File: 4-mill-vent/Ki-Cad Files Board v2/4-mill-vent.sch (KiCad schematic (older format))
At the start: 73 parts, among them J1 Fan, J2 Buzzer, J3 Power, J4 ICSP, J9 Mounting holes, Q3 PZT3904, Q4 PZT3904, Q5 TSM480P06CP, Q6 MMBT3904, SW1 Power_off, SW2 Power_On, SW3 Fan_Down, SW4 Fan_Up, U1 LM321, U2 ATmega328P-AU, U3 TPSM84212EAB, U4 LM1117-5.0, Y1 16.000MHZ

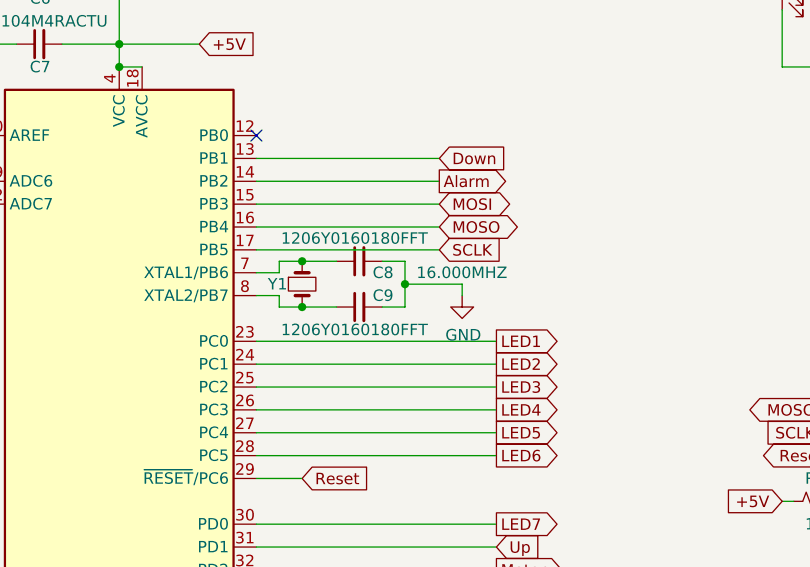
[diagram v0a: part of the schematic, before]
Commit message: Last Update USE V2
Board test complete, all slikscreen error are fixed in v2, Full use of opamp for battery monitoring.
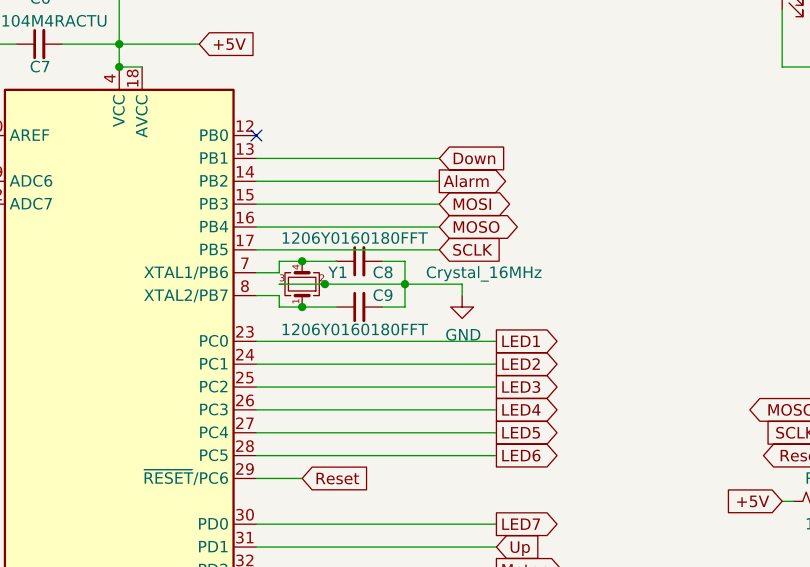
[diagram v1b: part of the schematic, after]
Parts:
- removed Y1: 16.000MHZ, Crystal:Crystal_SMD_0603-2Pin_6.0x3.5mm, symbol Device:Crystal_Small
- added Y1: Crystal_16MHz, Crystal:Crystal_SMD_0603-4Pin_6.0x3.5mm, symbol Device:Crystal_GND23_Small
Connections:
- net GND: now also Y1.2, Y1.3
- net at C8.1, U2.7 (XTAL1/PB6): now also Y1.4
- net at C9.1, U2.8 (XTAL2/PB7): now also Y1.1
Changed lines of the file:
@@
 $Descr B 17000 11000
 encoding utf-8
-Sheet 1 4
+Sheet 1 2
 Title ""
 Date ""
@@
 	1550 800  1950 800
 $Comp
-L MCU_Microchip_ATmega:ATmega328P-AU U2
-U 1 1 5F6A43BE
-P 1900 5300
-F 0 "U2" H 2700 3750 50  0000 C CNN
-F 1 "ATmega328P-AU" H 2750 3900 50  0000 C CNN
-F 2 "Package_QFP:TQFP-32_7x7mm_P0.8mm" H 1900 5300 50  0001 C CIN
-F 3 "http://ww1.microchip.com/downloads/en/DeviceDoc/ATmega328_P%20AVR%20MCU%20with%20picoPower%20Technology%20Data%20Sheet%2040001984A.pdf" H 1900 5300 50  0001 C CNN
-	1    1900 5300
-	1    0    0    -1
-$EndComp
-$Comp
 L power:GND #PWR013
 U 1 1 5F7FF4B2
@@
 	0    -1   -1   0
 $EndComp
-$Comp
-L Device:Crystal_Small Y1
-U 1 1 5F8CFD3F
-P 2700 4750
-F 0 "Y1" V 2700 4600 50  0000 L CNN
-F 1 "16.000MHZ" V 2650 5250 50  0000 L CNN
-F 2 "Crystal:Crystal_SMD_0603-2Pin_6.0x3.5mm" H 2700 4750 50  0001 C CNN
-F 3 "~" H 2700 4750 50  0001 C CNN
-	1    2700 4750
-	0    1    1    0
-$EndComp
 Wire Wire Line
 	2500 4700 2600 4700
@@
 	2600 4700 2600 4650
 Wire Wire Line
-	2600 4650 2700 4650
-Connection ~ 2700 4650
-Wire Wire Line
-	2700 4650 2850 4650
-Wire Wire Line
 	2500 4800 2600 4800
 Wire Wire Line
 	2600 4800 2600 4850
-Wire Wire Line
-	2600 4850 2700 4850
-Connection ~ 2700 4850
-Wire Wire Line
-	2700 4850 2850 4850
 Wire Wire Line
 	3050 4650 3150 4650
@@
 	2500 5500 3550 5500
 Wire Wire Line
-	2500 5400 3550 5400
-Wire Wire Line
 	3300 4200 2500 4200
 Wire Wire Line
@@
 	3550 5800 2500 5800
 Wire Wire Line
-	2500 5900 3550 5900
-Wire Wire Line
 	3550 6000 2500 6000
 Wire Wire Line
-	2500 5300 3550 5300
-Wire Wire Line
 	1900 3700 2250 3700
 Wire Wire Line
@@
 Wire Wire Line
 	1900 3700 1900 3800
-Connection ~ 1900 3800
 $Comp
 L power:PWR_FLAG #FLG02
@@
 Text Notes 13500 8200 0    50   ~ 0
 Arduino Nano Mapping\n\n#define FAN_PWM_PIN                 5 \n#define BATTERY_LED_1_PIN           A0\n#define BATTERY_LED_2_PIN           A1\n#define BATTERY_LED_3_PIN           A2\n#define Error_LED_PIN                 A3\n#define MODE_LED_1_PIN              A4\n#define MODE_LED_2_PIN              A5\n#define MODE_LED_3_PIN              0\n#define BUZZER_PIN                  10\n#define VIBRATOR_PIN                 2\n#define Monitor_PIN                   7 \n#define FAN_RPM_PIN                 3\n#define Fan_Up_PIN                   1\n#define Fan_Down_PIN                 9
+$Comp
+L Device:Crystal_GND23_Small Y1
+U 1 1 5F5F52E8
+P 2700 4750
+F 0 "Y1" V 2750 4550 50  0000 L CNN
+F 1 "Crystal_16MHz" V 2750 3700 50  0000 L CNN
+F 2 "Crystal:Crystal_SMD_0603-4Pin_6.0x3.5mm" H 2700 4750 50  0001 C CNN
+F 3 "~" H 2700 4750 50  0001 C CNN
+	1    2700 4750
+	0    -1   -1   0
+$EndComp
+Wire Wire Line
+	2600 4650 2700 4650
+Wire Wire Line
+	2600 4850 2700 4850
+Connection ~ 2700 4650
+Wire Wire Line
+	2700 4650 2850 4650
+Connection ~ 2700 4850
+Wire Wire Line
+	2700 4850 2850 4850
+Wire Wire Line
+	2800 4750 2600 4750
+Connection ~ 2800 4750
+Wire Wire Line
+	2800 4750 3150 4750
+Connection ~ 1900 3800
+Wire Wire Line
+	2500 5300 3550 5300
+Wire Wire Line
+	2500 5400 3550 5400
+Wire Wire Line
+	2500 5900 3550 5900
+$Comp
+L MCU_Microchip_ATmega:ATmega328P-AU U2
+U 1 1 5F6A43BE
+P 1900 5300
+F 0 "U2" H 2700 3750 50  0000 C CNN
+F 1 "ATmega328P-AU" H 2750 3900 50  0000 C CNN
+F 2 "Package_QFP:TQFP-32_7x7mm_P0.8mm" H 1900 5300 50  0001 C CIN
+F 3 "http://ww1.microchip.com/downloads/en/DeviceDoc/ATmega328_P%20AVR%20MCU%20with%20picoPower%20Technology%20Data%20Sheet%2040001984A.pdf" H 1900 5300 50  0001 C CNN
+	1    1900 5300
+	1    0    0    -1
+$EndComp
 $EndSCHEMATC
